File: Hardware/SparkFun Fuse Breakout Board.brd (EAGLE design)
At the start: 61.1 x 12.7 mm, 23 parts, among them J3 POWER_JACKPTH_LOCK

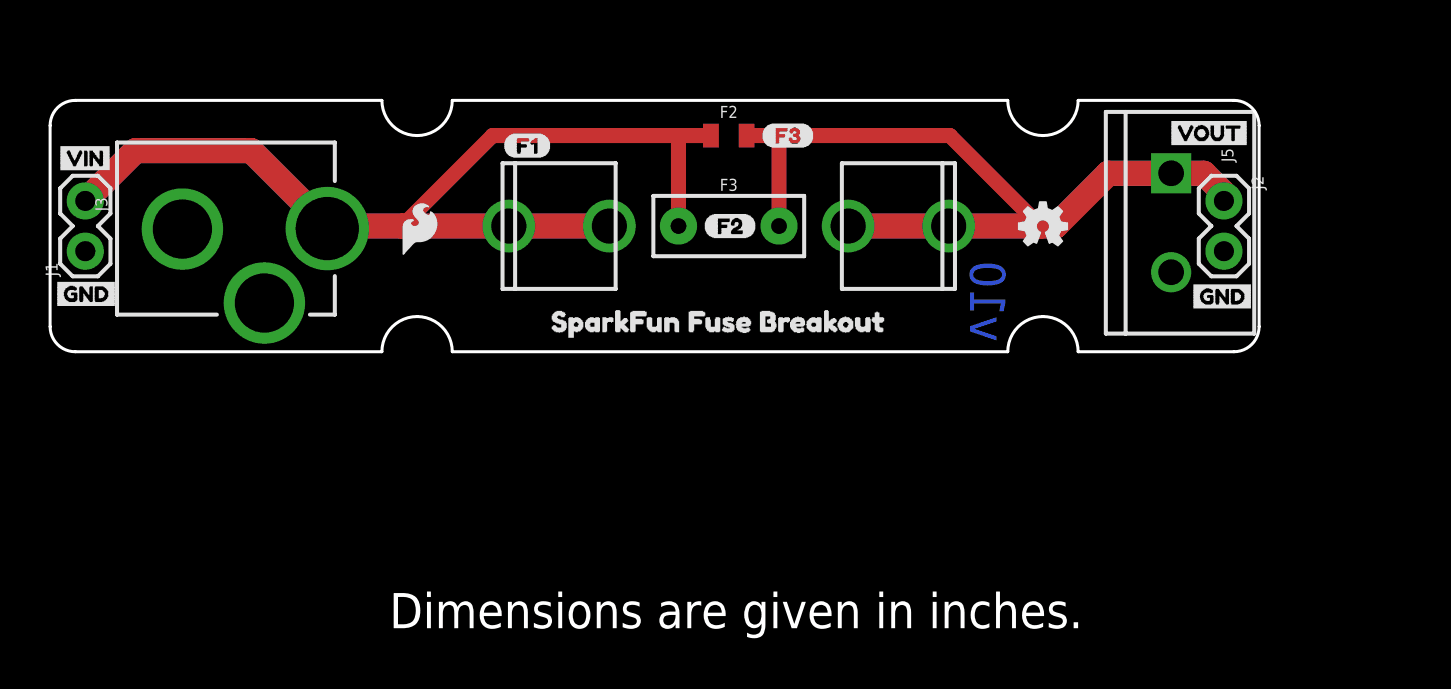
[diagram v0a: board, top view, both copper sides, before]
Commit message: Update board
- rotate version number
- split top polygon layer to VIN and VOUT
- add t-stop isolate with screw terminals
- remove SMD Fuse
- remove 0.1" PTH pins
- use screw terminal instead of PTH pins
- adjust board size to accomodate screw terminals
- +/- label behind screw terminal output
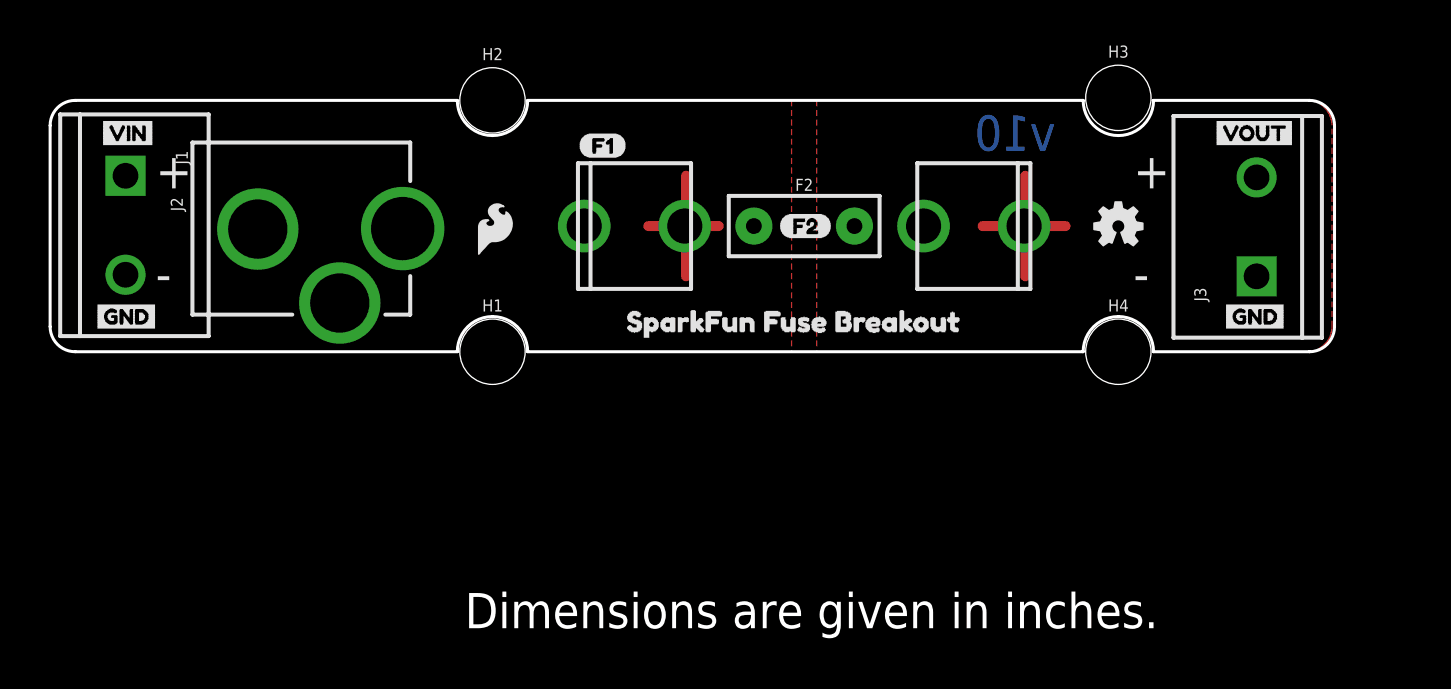
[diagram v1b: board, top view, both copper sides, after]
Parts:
- removed F3: 72V/0.25A, SparkFun-Fuses:PTH
- removed J5: (no value), SparkFun-Connectors:SCREWTERMINAL-5MM-2
- removed U$30: (no value), buzzard_labels (15):F30
- added H1, H2, H3, H4: STAND-OFF, SparkFun-Hardware:STAND-OFF
- F2: value 6V 0.5A -> 72V/0.25A; device SparkFun-Fuses:0805 -> SparkFun-Fuses:PTH
- J1: device SparkFun-Connectors:1X02 -> SparkFun-Connectors:SCREWTERMINAL-5MM-2
- J2: value (none) -> POWER_JACKPTH_LOCK; device SparkFun-Connectors:1X02 -> SparkFun-Connectors:POWER_JACK_PTH_LOCK
- J3: value POWER_JACKPTH_LOCK -> (none); device SparkFun-Connectors:POWER_JACK_PTH_LOCK -> SparkFun-Connectors:SCREWTERMINAL-5MM-2
- moved J3 60.9 mm to (61.0, 3.81), turned to 90 degrees
- moved J2 55.4 mm to (3.94, 6.22)
- moved F2 5.95 mm to (38.1, 6.35)
- moved J1 4.32 mm to (3.81, 8.89), turned to 270 degrees
- moved F1 3.81 mm to (38.1, 6.35)
- moved LOGO3 3.81 mm to (54.0, 6.35)
- moved U$28 3.81 mm to (26.7, 10.4)
- moved LOGO2 3.81 mm to (21.3, 4.57)
- moved U$11 3.81 mm to (28.2, 1.52)
- moved LOGO1 3.81 mm to (36.1, 0.76)
- moved U$29 3.81 mm to (36.8, 6.35)
- moved FRAME1 2.54 mm to (12.1, -24.1)
- moved U$14 2.50 mm to (5.59, 11.0)
- moved U$5 2.50 mm to (2.29, 11.0)
- moved U$2 2.44 mm to (5.71, 1.78)
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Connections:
- net GND: now also J2.GND, J2.GNDBREAK, J3.1; no longer J2.2, J3.GND, J3.GNDBREAK, J5.2
- net VIN: now also F2.P$1, J2.PWR; no longer F2.1, F3.P$1, J3.PWR
- net VOUT: now also F2.P$2, J3.2; no longer F2.2, F3.P$2, J2.1, J5.1
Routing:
- net VIN: track 79.8 -> 8.64 mm
- net VOUT: track 63.2 -> 9.27 mm
- added copper zone on layer 1, net VIN
- added copper zone on layer 1, net VOUT
- removed copper zone on layer 1, net GND
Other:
- board size 61.1 x 12.7 mm -> 64.9 x 12.7 mm
- board text added: "+"
- board text added: "-"

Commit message: Update Board
- move silkscreen for screw terminals
- remove stand offs and add top/bottom restrict for half mounting holes
- adjust isolation for polygon pours
- adjust polygon pour width for VIN and VOUT by F2
- big buzzard labels for VIN and VOUT
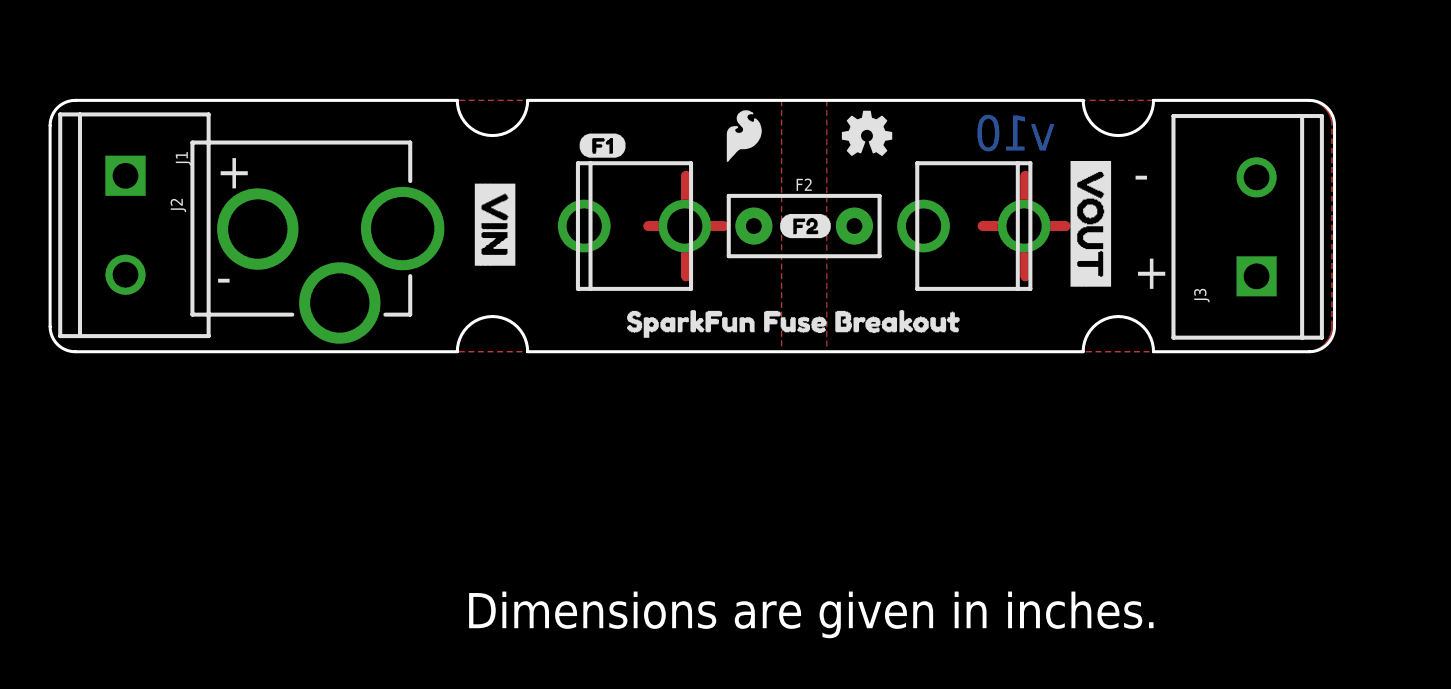
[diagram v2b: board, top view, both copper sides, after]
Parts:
- removed H1, H2, H3, H4: STAND-OFF, SparkFun-Hardware:STAND-OFF
- removed U$14, U$5: (no value), buzzard_labels (19):VIN0
- removed U$15, U$6: (no value), buzzard_labels (20):VOUT0
- removed U$20, U$21: (no value), buzzard_labels (18):GND0
- added U$3: (no value), buzzard_labels (1):VOUT0
- added U$4: (no value), buzzard_labels (2):VIN0
- U$1: device buzzard_labels (18):GND0 -> buzzard_labels (2):VIN0
- U$2: device buzzard_labels (18):GND0 -> buzzard_labels (1):VOUT0
- moved U$2 47.6 mm to (52.6, 10.3), flipped to the top, turned to 270 degrees
- moved U$1 21.7 mm to (22.5, 9.14), turned to 270 degrees
- moved LOGO3 13.5 mm to (41.3, 10.9)
- moved LOGO2 13.4 mm to (33.9, 9.27)
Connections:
- net GND: now also J1.2, J3.2; no longer J1.1, J3.1
- net VIN: now also J1.1; no longer J1.2
- net VOUT: now also J3.1; no longer J3.2
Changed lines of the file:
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@@
 <dimension x1="0" y1="0" x2="22.225" y2="0" x3="11.1125" y3="-3.81" textsize="1.778" textratio="15" layer="47" unit="inch"/>
 <text x="20.955" y="-13.97" size="1.778" layer="20" font="vector" ratio="15">Dimensions are given in inches.</text>
-<text x="54.737" y="8.255" size="1.778" layer="21" font="vector" ratio="15">+</text>
-<text x="54.737" y="3.048" size="1.778" layer="21" font="vector" ratio="15">-</text>
-<text x="56.007" y="8.255" size="1.778" layer="22" font="vector" ratio="15" rot="MR0">+</text>
-<text x="56.007" y="3.048" size="1.778" layer="22" font="vector" ratio="15" rot="MR0">-</text>
-<text x="5.334" y="8.255" size="1.778" layer="21" font="vector" ratio="15">+</text>
-<text x="5.334" y="3.048" size="1.778" layer="21" font="vector" ratio="15">-</text>
+<text x="54.737" y="3.175" size="1.778" layer="21" font="vector" ratio="15">+</text>
+<text x="54.737" y="8.128" size="1.778" layer="21" font="vector" ratio="15">-</text>
+<text x="56.007" y="3.175" size="1.778" layer="22" font="vector" ratio="15" rot="MR0">+</text>
+<text x="56.007" y="8.128" size="1.778" layer="22" font="vector" ratio="15" rot="MR0">-</text>
+<text x="8.382" y="8.255" size="1.778" layer="21" font="vector" ratio="15">+</text>
+<text x="8.382" y="2.921" size="1.778" layer="21" font="vector" ratio="15">-</text>
 <text x="6.604" y="8.255" size="1.778" layer="22" font="vector" ratio="15" rot="MR0">+</text>
 <text x="6.604" y="3.048" size="1.778" layer="22" font="vector" ratio="15" rot="MR0">-</text>
+<circle x="22.352" y="0" radius="2.83980625" width="0.1524" layer="41"/>
+<circle x="22.352" y="12.7" radius="2.83980625" width="0.1524" layer="41"/>
+<circle x="53.975" y="12.827" radius="2.83980625" width="0.1524" layer="41"/>
+<circle x="53.975" y="0" radius="2.83980625" width="0.1524" layer="41"/>
+<circle x="22.352" y="12.7" radius="2.83980625" width="0.1524" layer="42"/>
+<circle x="22.352" y="0" radius="2.83980625" width="0.1524" layer="42"/>
+<circle x="53.975" y="12.827" radius="2.83980625" width="0.1524" layer="42"/>
+<circle x="53.975" y="0" radius="2.83980625" width="0.1524" layer="42"/>
 </plain>
 <attributes>
@@
 </element>
 <element name="LOGO1" library="SparkFun-Aesthetics" package="SFE_LOGO_NAME_FLAME_.1" value="SFE_LOGO_NAME_FLAME.1_INCH" x="36.068" y="0.762" rot="MR90"/>
-<element name="LOGO2" library="SparkFun-Aesthetics" package="SFE_LOGO_FLAME_.1" value="SFE_LOGO_FLAME.1_INCH" x="21.336" y="4.572"/>
-<element name="LOGO3" library="SparkFun-Aesthetics" package="OSHW-LOGO-MINI" value="OSHW-LOGOMINI" x="53.975" y="6.35"/>
-<element name="U$5" library="buzzard_labels (19)" package="VIN0" value="" x="2.286" y="11.049"/>
-<element name="U$6" library="buzzard_labels (20)" package="VOUT0" value="" x="58.547" y="11.049"/>
+<element name="LOGO2" library="SparkFun-Aesthetics" package="SFE_LOGO_FLAME_.1" value="SFE_LOGO_FLAME.1_INCH" x="33.909" y="9.271"/>
+<element name="LOGO3" library="SparkFun-Aesthetics" package="OSHW-LOGO-MINI" value="OSHW-LOGOMINI" x="41.275" y="10.922"/>
 <element name="U$11" library="buzzard_labels (7)" package="SPARKFUN_FUSE_BREAKOUT0" value="" x="28.194" y="1.524"/>
-<element name="U$14" library="buzzard_labels (19)" package="VIN0" value="" x="5.588" y="11.049" rot="MR0"/>
-<element name="U$15" library="buzzard_labels (20)" package="VOUT0" value="" x="63.119" y="11.049" rot="MR0"/>
-<element name="U$1" library="buzzard_labels (18)" package="GND0" value="" x="2.032" y="1.778"/>
-<element name="U$2" library="buzzard_labels (18)" package="GND0" value="" x="5.715" y="1.778" rot="MR0"/>
-<element name="U$20" library="buzzard_labels (18)" package="GND0" value="" x="59.055" y="1.778"/>
-<element name="U$21" library="buzzard_labels (18)" package="GND0" value="" x="62.738" y="1.778" rot="MR0"/>
 <element name="U$28" library="buzzard_labels (17)" package="F10" value="" x="26.67" y="10.414"/>
 <element name="U$29" library="buzzard_labels (16)" package="F20" value="" x="36.83" y="6.35"/>
@@
 <attribute name="SF_SKU" value="PRT-08432" x="60.96" y="3.81" size="1.778" layer="27" rot="R90" display="off"/>
 </element>
-<element name="H1" library="SparkFun-Hardware" package="STAND-OFF" value="STAND-OFF" x="22.352" y="0"/>
-<element name="H2" library="SparkFun-Hardware" package="STAND-OFF" value="STAND-OFF" x="22.352" y="12.7"/>
-<element name="H3" library="SparkFun-Hardware" package="STAND-OFF" value="STAND-OFF" x="53.975" y="12.827"/>
-<element name="H4" library="SparkFun-Hardware" package="STAND-OFF" value="STAND-OFF" x="53.975" y="0"/>
+<element name="U$2" library="buzzard_labels (1)" package="VOUT0" value="" x="52.578" y="10.287" rot="R270"/>
+<element name="U$1" library="buzzard_labels (2)" package="VIN0" value="" x="22.479" y="9.144" rot="R270"/>
+<element name="U$3" library="buzzard_labels (1)" package="VOUT0" value="" x="52.578" y="10.287" rot="MR270"/>
+<element name="U$4" library="buzzard_labels (2)" package="VIN0" value="" x="22.479" y="9.144" rot="MR270"/>
 </elements>
 <signals>
 <signal name="GND">
-<polygon width="0.254" layer="16">
+<polygon width="0.254" layer="16" isolate="0.508">
 <vertex x="52.197" y="12.7"/>
 <vertex x="24.13" y="12.7" curve="-90"/>
@@
 <contactref element="J2" pad="GND"/>
 <contactref element="J2" pad="GNDBREAK"/>
-<contactref element="J1" pad="1"/>
-<contactref element="J3" pad="1"/>
+<contactref element="J1" pad="2"/>
+<contactref element="J3" pad="2"/>
 </signal>
 <signal name="VIN">
 <contactref element="F1" pad="1"/>
 <contactref element="F2" pad="P$1"/>
-<contactref element="J2" pad="PWR"/>
-<contactref element="J1" pad="2"/>
-<polygon width="0.254" layer="1" isolate="0.254">
-<vertex x="37.465" y="0"/>
+<polygon width="0.254" layer="1" isolate="0.508">
+<vertex x="36.957" y="0"/>
 <vertex x="1.27" y="0" curve="-90"/>
 <vertex x="0" y="1.27"/>
 <vertex x="0" y="11.43" curve="-90"/>
 <vertex x="1.27" y="12.7"/>
-<vertex x="37.465" y="12.7"/>
+<vertex x="36.957" y="12.7"/>
 </polygon>
 <wire x1="32.131" y1="3.81" x2="32.131" y2="8.89" width="0.508" layer="1"/>
-<wire x1="30.226" y1="6.35" x2="33.782" y2="6.35" width="0.508" layer="1"/>
+<wire x1="30.226" y1="6.35" x2="34.036" y2="6.35" width="0.508" layer="1"/>
+<contactref element="J2" pad="PWR"/>
+<contactref element="J1" pad="1"/>
 </signal>
 <signal name="VOUT">
-<polygon width="0.254" layer="1" isolate="0.254">
-<vertex x="38.735" y="0"/>
+<polygon width="0.254" layer="1" isolate="0.508">
+<vertex x="39.243" y="0"/>
 <vertex x="63.5" y="0" curve="90"/>
 <vertex x="64.77" y="1.27"/>
 <vertex x="64.77" y="11.43" curve="90"/>
 <vertex x="63.5" y="12.7"/>
-<vertex x="38.735" y="12.7"/>
+<vertex x="39.243" y="12.7"/>
 </polygon>
 <contactref element="F2" pad="P$2"/>
 <contactref element="F1" pad="3"/>
-<contactref element="J3" pad="2"/>
 <wire x1="51.308" y1="6.35" x2="47.117" y2="6.35" width="0.508" layer="1"/>
 <wire x1="49.276" y1="3.81" x2="49.276" y2="8.89" width="0.508" layer="1"/>
+<contactref element="J3" pad="1"/>
 </signal>
 </signals>
+<errors>
+</errors>
 </board>
 </drawing>

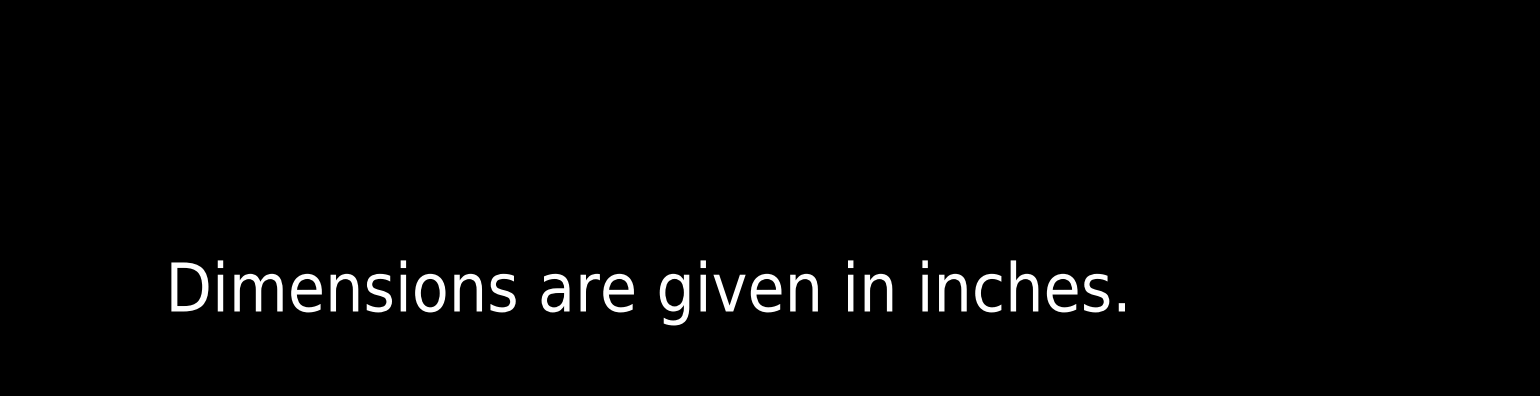
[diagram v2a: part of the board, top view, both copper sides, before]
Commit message: Update SparkFun Fuse Breakout Board.brd
- rotate label on back to match SFE logo
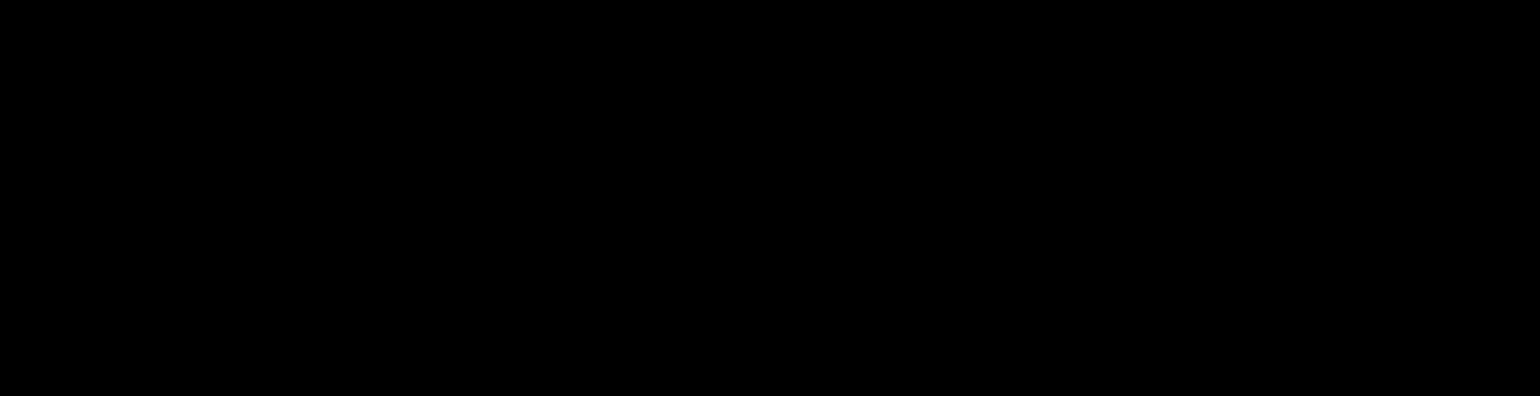
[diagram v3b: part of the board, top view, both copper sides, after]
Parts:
- moved U$3 7.62 mm to (52.6, 2.67), turned to 90 degrees
- moved U$4 5.46 mm to (22.5, 3.68), turned to 90 degrees
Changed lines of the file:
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@@
 <dimension x1="0" y1="0" x2="64.897" y2="0" x3="32.4485" y3="-8.89" textsize="1.778" textratio="15" layer="47" unit="inch"/>
 <dimension x1="0" y1="0" x2="22.225" y2="0" x3="11.1125" y3="-3.81" textsize="1.778" textratio="15" layer="47" unit="inch"/>
-<text x="20.955" y="-13.97" size="1.778" layer="20" font="vector" ratio="15">Dimensions are given in inches.</text>
+<text x="20.955" y="-13.97" size="1.778" layer="47" font="vector" ratio="15">Dimensions are given in inches.</text>
 <text x="54.737" y="3.175" size="1.778" layer="21" font="vector" ratio="15">+</text>
 <text x="54.737" y="8.128" size="1.778" layer="21" font="vector" ratio="15">-</text>
@@
 <element name="U$2" library="buzzard_labels (1)" package="VOUT0" value="" x="52.578" y="10.287" rot="R270"/>
 <element name="U$1" library="buzzard_labels (2)" package="VIN0" value="" x="22.479" y="9.144" rot="R270"/>
-<element name="U$3" library="buzzard_labels (1)" package="VOUT0" value="" x="52.578" y="10.287" rot="MR270"/>
-<element name="U$4" library="buzzard_labels (2)" package="VIN0" value="" x="22.479" y="9.144" rot="MR270"/>
+<element name="U$3" library="buzzard_labels (1)" package="VOUT0" value="" x="52.578" y="2.667" rot="MR90"/>
+<element name="U$4" library="buzzard_labels (2)" package="VIN0" value="" x="22.479" y="3.683" rot="MR90"/>
 </elements>
 <signals>
